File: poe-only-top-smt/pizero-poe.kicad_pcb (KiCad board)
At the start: 2 copper layers, 81.8 x 30 mm, 77 parts, among them IC1 ENC28J60-I/ML, J1 RJ45-LED, P1 Raspberry_Pi_+_Conn, P2 WS2812 Cn., P3 WS2812 Cn., Q1 SI3440DV, Q2 BSS138, Q3 BSS138, T1 PULSE_H1197, T2 TRANSFO, T3 VOLTAGE_REF, U1 LTC4267, U2 PAS291, U3 LM1117IMPX-ADJ, U5 DMMT5401, Y1 25Mhz

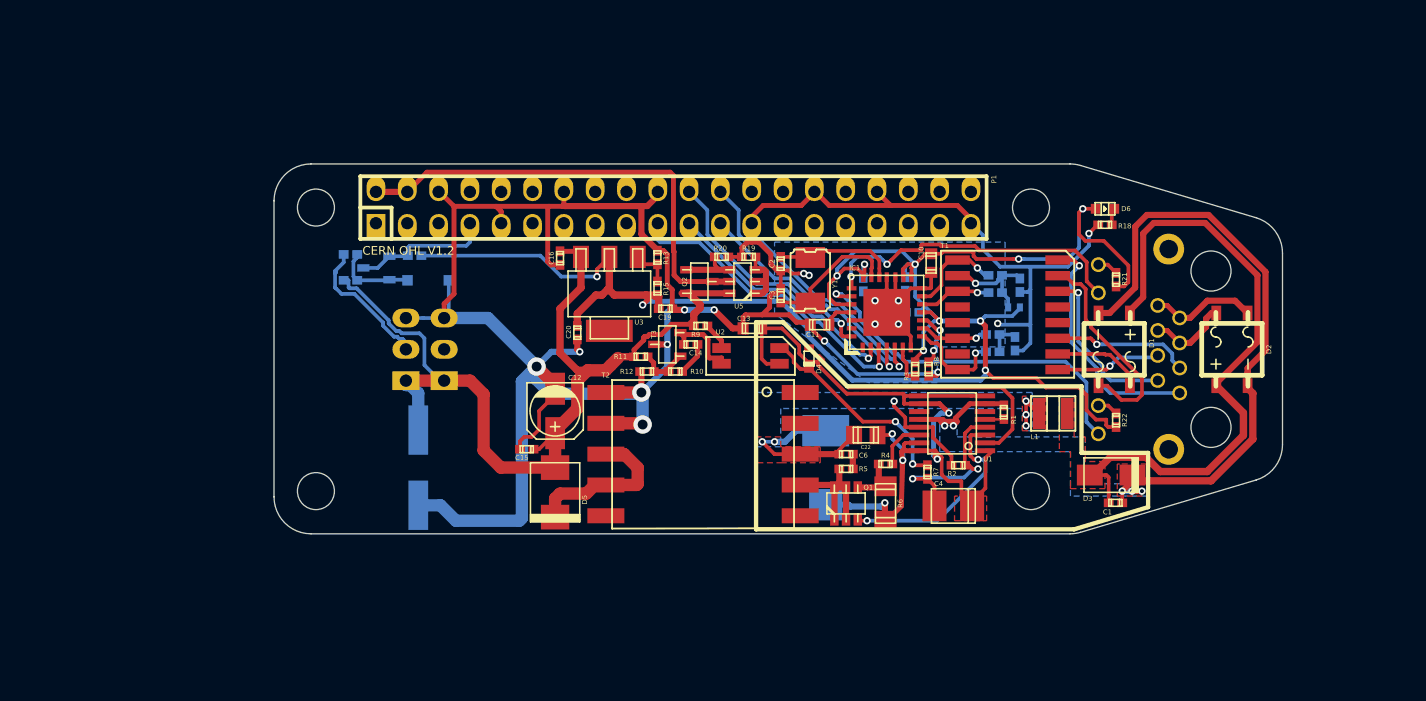
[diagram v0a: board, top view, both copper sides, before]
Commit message: use rpi interface from ihartwig/raspberrypi-debugger and footprints from kicad 4+
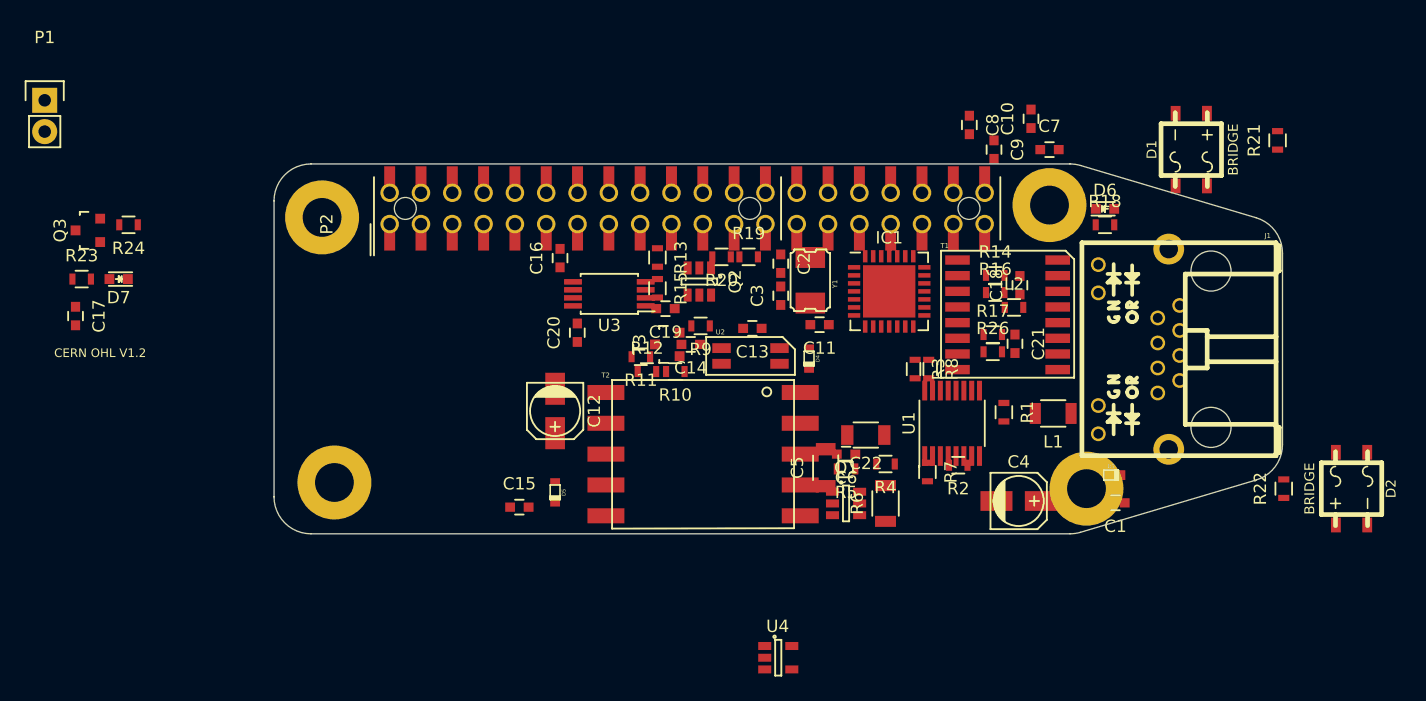
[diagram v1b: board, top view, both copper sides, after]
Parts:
- removed MT1, MT2, MT3, MT4: MountingHole_3mm, Mounting_Holes:MountingHole_3mm
- removed P3: WS2812 Cn., w_pin_strip:pin_strip_3-90
- removed R25: 100, w_smd_resistors:r_0402
- removed U5: DMMT5401, w_smd_trans:sot23-6
- added H1: hole-metalized-no4, pizero-poe-special:hole-m3, F.Cu at (111.1, 103.7)
- added H2: hole-metalized-no4, pizero-poe-special:hole-m3, F.Cu at (110.1, 82.2)
- added H3: hole-metalized-no4, pizero-poe-special:hole-m3, F.Cu at (172.1, 104.2)
- added H4: hole-metalized-no4, pizero-poe-special:hole-m3, F.Cu at (169.1, 81.2)
- added U4: AP7365_SOT-23-5, TO_SOT_Packages_SMD:SOT-23-5, F.Cu at (147.1, 117.9)
- C1, C2, C3, C6: footprint w_smd_cap:c_0402 -> Capacitors_SMD:C_0603
- C10, C11, C13: footprint w_smd_cap:c_0603 -> Capacitors_SMD:C_0603
- C12: footprint w_smd_cap:c_elec_4x4.5 -> Capacitors_SMD:c_elec_4x4.5
- C14: value C -> 6.8nf; footprint w_smd_cap:c_0402 -> Capacitors_SMD:C_0603
- C15, C16: value C -> 0.1uf; footprint w_smd_cap:c_0402 -> Capacitors_SMD:C_0603
- C17: value CP -> dnp-100n; footprint w_smd_cap:c_elec_8x6.5 -> Capacitors_SMD:C_0603; moved to F.Cu
- C18, C21, C7, C8, C9: footprint w_smd_cap:c_0402 -> Capacitors_SMD:C_0603; moved to F.Cu
- C19: value 0.1uf -> 1uF; footprint w_smd_cap:c_0402 -> Capacitors_SMD:C_0603
- C20: value 1uf -> 1uF; footprint w_smd_cap:c_0402 -> Capacitors_SMD:C_0603
- C22: footprint w_smd_cap:c_0805 -> Capacitors_SMD:C_1206
- C4: footprint w_smd_cap:c_tant_B -> Capacitors_SMD:c_elec_4x4.5
- C5: footprint w_smd_cap:c_tant_D -> Capacitors_SMD:C_1206; moved to F.Cu
- D1, D2: footprint w_smd_diode:MBS -> pizero-poe-special:MBS
- D3: footprint w_smd_diode:do214ac -> pizero-poe-special:sod523
- D4: footprint w_smd_diode:sod523 -> pizero-poe-special:sod523
- D5: footprint w_smd_diode:do214aa -> pizero-poe-special:sod523
- D6: value LED -> LED Green; footprint w_smd_leds:Led_0603 -> LEDs:LED_0603
- D7: value ZENER -> LED Green; footprint w_smd_diode:sod123 -> LEDs:LED_0603; moved to F.Cu
- IC1: footprint w_smd_qfn:qfn-28 -> Housings_DFN_QFN:QFN-28-1EP_6x6mm_Pitch0.65mm
- J1: moved to F.Cu
- L1: footprint w_smd_inductors:inductor_smd_1008 -> Resistors_SMD:R_1206
- L2: footprint w_smd_inductors:inductor_smd_0402 -> Resistors_SMD:R_0603; moved to F.Cu
- P1: value Raspberry_Pi_+_Conn -> dnp-CONN_01X02; footprint w_pin_strip:pin_socket_20x2 -> Pin_Headers:Pin_Header_Straight_1x02
- P2: value WS2812 Cn. -> dnp-REF-182665-01; footprint w_pin_strip:pin_strip_3 -> pizero-poe-special:Pin_Header_Straight_TH-SMT-NoPaste_2x20; moved to F.Cu
- Q1: footprint w_smd_trans:tsot-6 -> TO_SOT_Packages_SMD:SOT-23-6
- Q2: value BSS138 -> DMMT3906_Dual_PNP; footprint w_smd_trans:sot23 -> TO_SOT_Packages_SMD:SOT-23-6
- Q3: value BSS138 -> Q_PMOS_GSD; footprint w_smd_trans:sot23 -> TO_SOT_Packages_SMD:SOT-23; moved to F.Cu
- R1: value 68.1 -> DNP; footprint w_smd_resistors:r_0402 -> Resistors_SMD:R_0603
- R10, R11, R4: value R -> 10k; footprint w_smd_resistors:r_0402 -> Resistors_SMD:R_0603
- R12: value R -> 3.3k; footprint w_smd_resistors:r_0402 -> Resistors_SMD:R_0603
- R13: value 390 -> 1k; footprint w_smd_resistors:r_0402 -> Resistors_SMD:R_0603
- R14, R16, R17, R26: footprint w_smd_resistors:r_0402 -> Resistors_SMD:R_0603; moved to F.Cu
- R15: value 240 -> 10k; footprint w_smd_resistors:r_0402 -> Resistors_SMD:R_0603
- R18: value 360 -> dnp-1k; footprint w_smd_resistors:r_0402 -> Resistors_SMD:R_0603
- R19: value 10k -> 47k; footprint w_smd_resistors:r_0402 -> Resistors_SMD:R_0603
- R2, R21, R22, R3, R5, R8: footprint w_smd_resistors:r_0402 -> Resistors_SMD:R_0603
- R20: value 47k -> dnp-3.9k; footprint w_smd_resistors:r_0402 -> Resistors_SMD:R_0603
- R23: value 14k -> dnp-3.9k; footprint w_smd_resistors:r_0402 -> Resistors_SMD:R_0603; moved to F.Cu
- R24: value 14k -> 220; footprint w_smd_resistors:r_0402 -> Resistors_SMD:R_0603; moved to F.Cu
- R6: footprint w_smd_resistors:r_1206 -> Resistors_SMD:R_1206
- R7: value R -> 6.8k; footprint w_smd_resistors:r_0402 -> Resistors_SMD:R_0603
- R9: value R -> 1k; footprint w_smd_resistors:r_0402 -> Resistors_SMD:R_0603
- T3: footprint w_smd_trans:sot23 -> TO_SOT_Packages_SMD:SOT-23
- U1: footprint w_smd_dil:ssop-16 -> Housings_SSOP:QSOP-16_3.9x4.9mm_Pitch0.635mm
- U3: value LM1117IMPX-ADJ -> dnp-AT24CS32-SSHM; footprint w_smd_trans:sot223 -> Housings_SSOP:TSSOP-8_4.4x3mm_Pitch0.65mm
- moved P1 51.7 mm to (87.6, 72.7)
- moved C17 30.4 mm to (90.1, 90.2), turned to 270 degrees
- moved R23 27.1 mm to (90.6, 87.2)
- moved D7 25.1 mm to (93.6, 87.2)
- moved Q3 23.6 mm to (91.1, 83.2), turned to 90 degrees
- moved R24 18.6 mm to (94.4, 82.8)
- moved D1 17.4 mm to (180.6, 76.7)
- moved R21 17.3 mm to (187.6, 76.0)
- moved C7 17.2 mm to (169.1, 76.7)
- moved C8 15.5 mm to (162.6, 74.7), turned to 270 degrees
- moved D2 14.9 mm to (193.6, 104.2)
- moved R22 14.7 mm to (188.1, 104.2)
- moved C10 14.2 mm to (167.6, 74.2)
- moved C9 13.1 mm to (164.6, 76.7), turned to 270 degrees
- moved P2 11.1 mm to (115.6, 82.7)
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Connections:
- C17 pad 1: +5V -> /RPI_3V3_2
- C19 pad 1: +3V3 -> /RPI_VBUS
- D6 pad 1: +3V3 -> Net-(D6-Pad1)
- D6 pad 2: Net-(D6-Pad2) -> +5V
- D7 pad 1: GND -> Net-(D7-Pad1)
- D7 pad 2: Net-(D7-Pad2) -> +3V3
- IC1 pad 1: /ENC_WOL -> (no net)
- IC1 pad 2: /ENC_SO -> /GPIO9_MISO
- IC1 pad 27: Net-(IC1-Pad27) -> (no net)
- IC1 pad 28: /ENC_INT -> (no net)
- IC1 pad 29: (no net) -> GND
- IC1 pad 3: /ENC_SI -> /GPIO10_MOSI
- IC1 pad 4: /ENC_SCK -> /GPIO11_SCLK
- IC1 pad 5: /ENC_CS -> /GPIO8_CE0#
- P1 pad 2: /sheet56B34F8B/5V_MCU -> GND
- P2 pad 1: +5V -> /RPI_3V3_1
- P2 pad 2: Net-(P2-Pad2) -> /RPI_VBUS
- P2 pad 3: GND -> /GPIO1_SDA1
- Q2 pad 1: Net-(Q2-Pad1) -> +5V
- Q2 pad 2: /sheet56B34F8B/5V_MCU -> (no net)
- Q2 pad 3: +5V -> /RPI_VBUS
- Q3 pad 1: /WS2812_DO -> Net-(Q2-Pad4)
- Q3 pad 2: /WS2812_DO -> /RPI_VBUS
- Q3 pad 3: Net-(D7-Pad2) -> +5V
- R13 pad 1: Net-(R13-Pad1) -> Net-(D6-Pad1)
- R15 pad 1: +3V3 -> Net-(Q2-Pad5)
- R15 pad 2: Net-(R13-Pad1) -> GND
- R18 pad 1: Net-(D6-Pad2) -> /RPI_3V3_2
- R18 pad 2: GND -> Net-(P1-Pad1)
- R19 pad 1: Net-(R19-Pad1) -> Net-(Q2-Pad4)
- R20 pad 1: Net-(Q2-Pad1) -> /RPI_3V3_2
- R20 pad 2: GND -> /GPIO0_ID_SD
- R23 pad 1: +3V3 -> /RPI_3V3_2
- R23 pad 2: /WS2812_DO -> /GPIO1_ID_SC
- R24 pad 1: +5V -> Net-(D7-Pad1)
- R24 pad 2: Net-(D7-Pad2) -> GND
- T1 pad 7: Net-(T1-Pad7) -> (no net)
- U1 pad 11: Net-(U1-Pad11) -> (no net)
- U3 pad 1: Net-(R13-Pad1) -> GND
- U3 pad 2: +3V3 -> GND
- U3 pad 3: +5V -> GND
- U3 pad 4: (no net) -> GND
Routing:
- net GND: track 227.9 -> 0.00 mm, vias 16 -> 0
- net +3V3: track 149.6 -> 0.00 mm, vias 11 -> 0
- net +5V: track 79.2 -> 0.00 mm
- net GNDPWR: track 72.7 -> 0.00 mm, vias 5 -> 0
- net Net-(C1-Pad2): track 63.6 -> 0.00 mm, vias 5 -> 0
- net Net-(C1-Pad1): track 52.0 -> 0.00 mm
- net /sheet56B34F8B/5V_MCU: track 37.7 -> 0.00 mm
- net /LEDA_CATH: track 29.5 -> 0.00 mm, vias 1 -> 0
- net Net-(C22-Pad1): track 26.2 -> 0.00 mm, vias 6 -> 0
- net /LEDB_CATH: track 26.1 -> 0.00 mm, vias 2 -> 0
- net /ENC_SI: track 25.2 -> 0.00 mm, vias 1 -> 0
- net Net-(D4-Pad1): track 23.5 -> 0.00 mm
- net /ENC_CS: track 23.5 -> 0.00 mm, vias 1 -> 0
- net /ENC_SCK: track 20.9 -> 0.00 mm, vias 1 -> 0
- net /ENC_SO: track 20.1 -> 0.00 mm, vias 1 -> 0
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- removed copper zone on B.Cu, net GND
- removed copper zone on F.Cu, net Net-(C1-Pad1)
- removed copper zone on B.Cu, net Net-(C1-Pad2)
- removed copper zone on F.Cu, net Net-(C1-Pad2)
- removed copper zone on B.Cu, net Net-(C22-Pad1)
- removed copper zone on F.Cu, net Net-(C22-Pad1)
- removed copper zone on F.Cu, net Net-(C5-Pad1)
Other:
- board text removed: "+5V"
- board text removed: "DO"
- board text removed: "GND"
- board text removed: "To Do: - check all diodes to see if they are reversed - create labeling for PoEPi - check schematic and PoE ciruit for errors"
- board text removed: "WS2812 DRIVER"

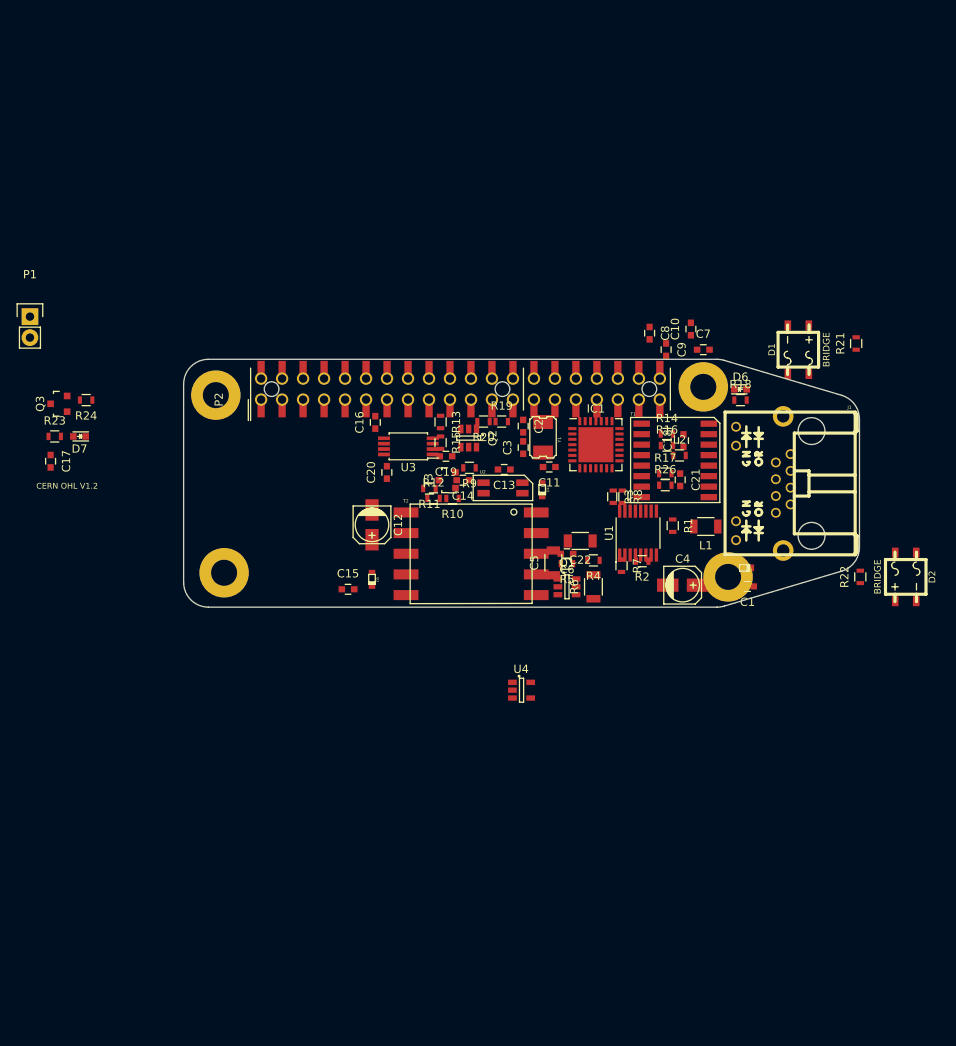
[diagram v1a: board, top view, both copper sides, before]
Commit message: refresh parts on pcb and separate functional groups
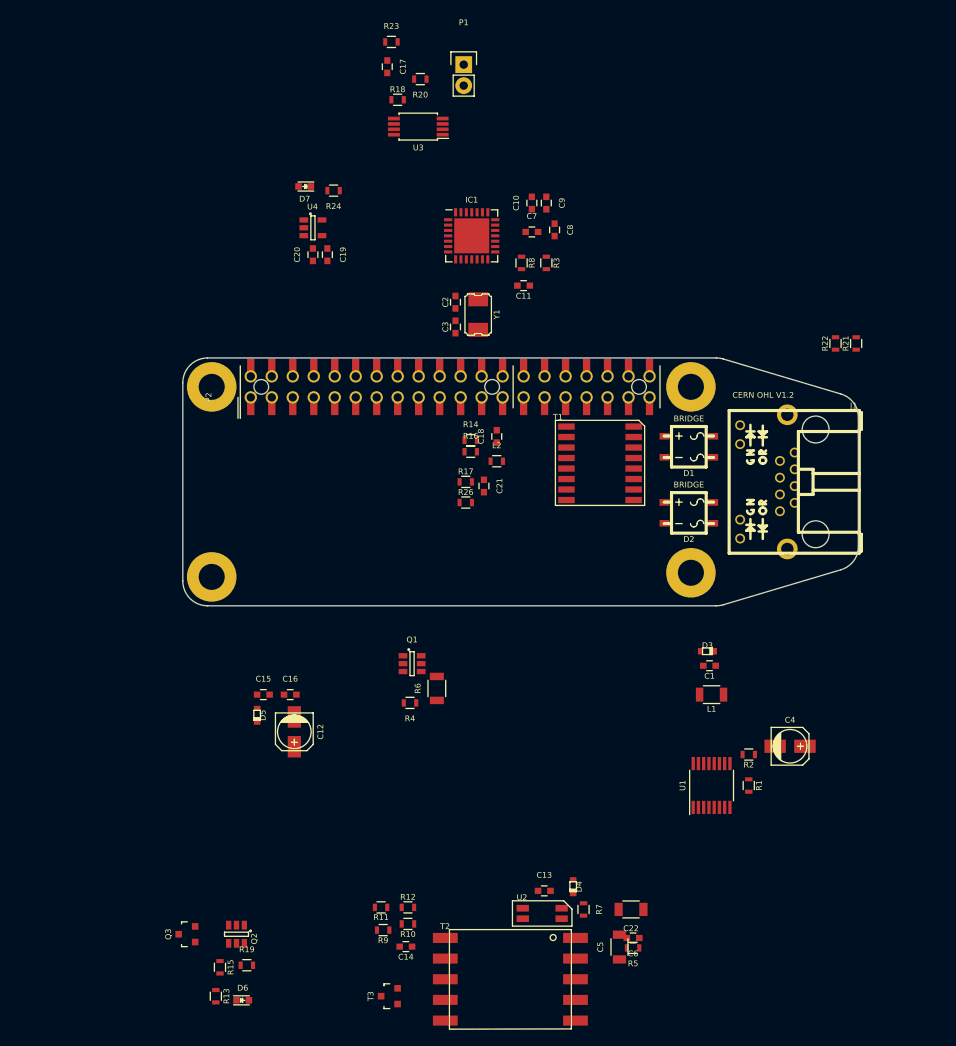
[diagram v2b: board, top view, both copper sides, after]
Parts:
- moved D6 95.4 mm to (113.3, 155.4)
- moved R13 74.6 mm to (110.1, 154.9)
- moved R19 72.7 mm to (113.8, 151.2)
- moved R15 68.9 mm to (110.6, 151.4)
- moved Q2 66.3 mm to (112.6, 147.4)
- moved Q3 66.0 mm to (106.6, 147.4)
- moved T3 62.8 mm to (131.1, 154.9)
- moved C17 62.8 mm to (130.8, 42.5)
- moved R23 62.8 mm to (131.3, 39.5)
- moved U4 61.4 mm to (121.8, 62.0)
- moved P1 60.7 mm to (140.1, 42.2)
- moved R9 56.9 mm to (130.3, 146.9)
- moved C14 56.9 mm to (133.1, 148.9)
- moved R18 55.2 mm to (132.1, 46.5)
- moved R10 51.8 mm to (133.3, 146.2)
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
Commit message: floorplan, named nets, design rules set
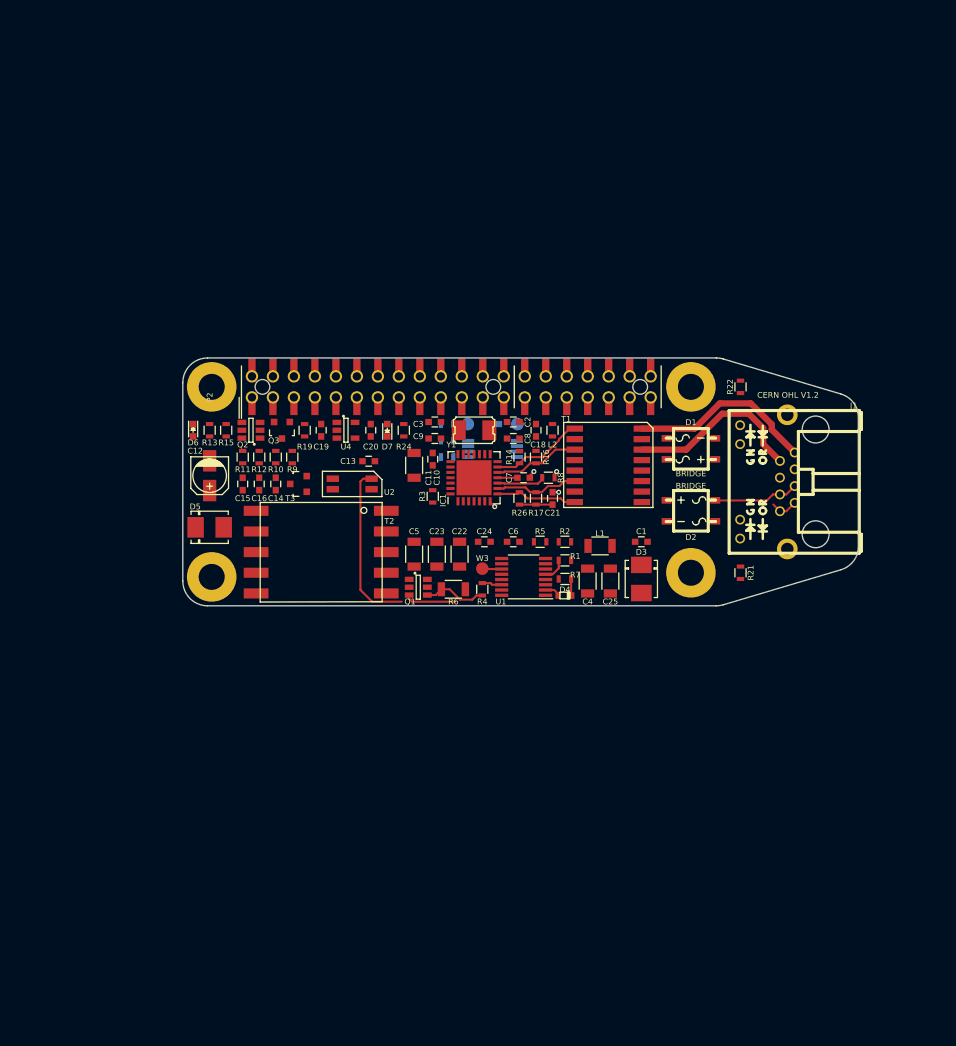
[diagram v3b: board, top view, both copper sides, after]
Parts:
- removed P1: dnp-CONN_01X02, Pin_Headers:Pin_Header_Straight_1x02
- added C23: 2.2uF 100V, Capacitors_SMD:C_1206, F.Cu at (136.8, 101.5)
- added C24: 0.1uF 100V, Capacitors_SMD:C_0603, F.Cu at (142.6, 100.0)
- added C25: 2.2uF 100V, Capacitors_SMD:C_1206, F.Cu at (157.8, 104.7)
- added W1: TEST_1P, Measurement_Points:Measurement_Point_Round-SMD-Pad_Small, B.Cu at (146.6, 85.7)
- added W2: TEST_1P, Measurement_Points:Measurement_Point_Round-SMD-Pad_Small, B.Cu at (140.6, 85.7)
- added W3: TEST_1P, Measurement_Points:Measurement_Point_Round-SMD-Pad_Small, F.Cu at (142.3, 103.2)
- C1: value 0.1uf -> 0.1uf 100V
- C11: footprint Capacitors_SMD:C_0603 -> Capacitors_SMD:C_1206
- C12: value CP -> 470uF
- C15, C16: value 0.1uf -> 0.1uF
- C17, R18, R20, R23, U3: moved to B.Cu
- C22: value 1uf -> 2.2uF 100V
- C4: value 220uf -> 2.2uF 100V; footprint Capacitors_SMD:c_elec_4x4.5 -> Capacitors_SMD:C_1206
- C5: value 6.8uf -> 2.2uF 100V
- C6: value C -> DNP
- D3: value ZENER -> SMAJ58A; footprint pizero-poe-special:sod523 -> Diodes_SMD:DO-214BA
- D5: value D_Schottky -> SBM1040; footprint pizero-poe-special:sod523 -> Diodes_SMD:DO-214BA
- R5: value R -> DNP
- moved D6 69.3 mm to (107.3, 86.5), turned to 270 degrees
- moved R13 68.5 mm to (109.3, 86.5)
- moved R19 65.1 mm to (120.8, 86.5), turned to 270 degrees
- moved R15 65.0 mm to (111.3, 86.5)
- moved T3 63.0 mm to (120.1, 93.0)
- moved Q3 62.1 mm to (118.1, 86.5), turned to 180 degrees
- moved Q2 61.0 mm to (114.3, 86.5), turned to 180 degrees
- moved R10 58.7 mm to (117.3, 89.7), turned to 270 degrees
- moved R9 58.3 mm to (119.3, 89.7), turned to 270 degrees
- moved C14 58.2 mm to (117.3, 93.0), turned to 90 degrees
- moved R12 57.4 mm to (115.3, 89.7), turned to 90 degrees
- moved R11 57.0 mm to (113.3, 89.7), turned to 270 degrees
- moved U2 56.8 mm to (126.6, 93.0)
- moved T2 56.5 mm to (122.8, 101.2)
- moved C13 56.2 mm to (128.6, 90.2)
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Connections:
- net /LEDA_CATH renamed /LEDA_K
- net /LEDB_CATH renamed /LEDB_K
- net /PVCC renamed /POE_PVCC
- net /RUN renamed /POE_RUN
- net Net-(C1-Pad1) renamed /POE_VPORTP_L
- net Net-(C1-Pad2) renamed /POE_VPORTN
- net Net-(C14-Pad1) renamed /POE_FB_K
- net Net-(C2-Pad2) renamed /PHY_OSC1
- net Net-(C22-Pad1) renamed /POE_VPORTP
- net Net-(C3-Pad2) renamed /PHY_OSC2
- net Net-(J1-Pad1) renamed /TPOUT_T+
- net Net-(J1-Pad10) renamed /LEDA_A
- net Net-(J1-Pad12) renamed /LEDB_A
- net Net-(J1-Pad2) renamed /TPOUT_T-
- net Net-(J1-Pad3) renamed /TPIN_T+
- net Net-(J1-Pad4) renamed /TPIN_T-
- net Net-(Q1-Pad1) renamed /POE_SW_D
- net Net-(Q1-Pad4) renamed /POW_SW_S
- net Net-(R10-Pad1) renamed /POE_FB_DIV
- net Net-(R4-Pad2) renamed /POE_SW_SENSE
- net Net-(R9-Pad2) renamed /POE_FB_A
- H1 pad 1: (no net) -> Net-(H1-Pad1)
- H2 pad 1: (no net) -> Net-(H2-Pad1)
- H3 pad 1: (no net) -> Net-(H3-Pad1)
- H4 pad 1: (no net) -> Net-(H4-Pad1)
- IC1 pad 1: (no net) -> Net-(IC1-Pad1)
- IC1 pad 27: (no net) -> Net-(IC1-Pad27)
- IC1 pad 28: (no net) -> /GPIO_25
- T1 pad 7: (no net) -> Net-(T1-Pad7)
- U1 pad 11: (no net) -> /~POE_PWRGD
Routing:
- net /TPOUT_T+: track 0.00 -> 22.6 mm
- net /POE_RUN: track 0.00 -> 22.2 mm
- net /TPOUT_T-: track 0.00 -> 22.0 mm
- net /TPOUT+: track 0.00 -> 11.3 mm
- net /TPOUT-: track 0.00 -> 10.5 mm
- net /SPARE_PAIR_1: track 0.00 -> 10.3 mm
- net /TPIN+: track 0.00 -> 10.2 mm
- net /TPIN-: track 0.00 -> 9.92 mm
- net /POW_SW_S: track 0.00 -> 7.66 mm
- net Net-(Q1-Pad3): track 0.00 -> 6.19 mm
- net Net-(IC1-Pad10): track 0.00 -> 5.83 mm
- net Net-(C21-Pad1): track 0.00 -> 4.00 mm
- net GND: track 0.00 -> 3.44 mm, vias 0 -> 4
- net /SPARE_PAIR_2: track 0.00 -> 3.33 mm
- net Net-(R1-Pad1): track 0.00 -> 2.85 mm
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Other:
- net class Default: clearance 0.15 -> 0.2032; trace_width 0.2 -> 0.254; via_dia 0.6 -> 0.6096; via_drill 0.32 -> 0.3048
- net class PoE Power added: clearance 0.254, trace_width 0.762, via_dia 0.6096, via_drill 0.3048
- net class Power added: clearance 0.2032, trace_width 0.308, via_dia 0.6096, via_drill 0.3048
- rule trace_clearance: 0.15 -> 0.2032
